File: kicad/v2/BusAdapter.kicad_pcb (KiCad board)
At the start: 2 copper layers, 99.1 x 99.1 mm, 55 parts, among them J1 Conn_02x17_Odd_Even, J10 Conn_02x06_Odd_Even, J11 Conn_02x02_Odd_Even, J12 Conn_02x06_Top_Bottom, J13 Conn_01x03, J14 Conn_01x02, J2 Conn_02x20_Odd_Even, J3 Conn_02x20_Odd_Even, J4 Conn_02x06_Top_Bottom, J5 Conn_02x06_Top_Bottom, J6 Conn_Coaxial, J7 Conn_Coaxial, J8 Conn_01x02_Male, J9 Conn_01x02_Male, Q1 2N3904, Q2 2N3904, SW1 SW_Push, SW2 SW_Push, U1 74LVC245, U2 74LVC245, U3 74LVC245, U4 IS61C5128AL-10TLI, U5 MCP4822

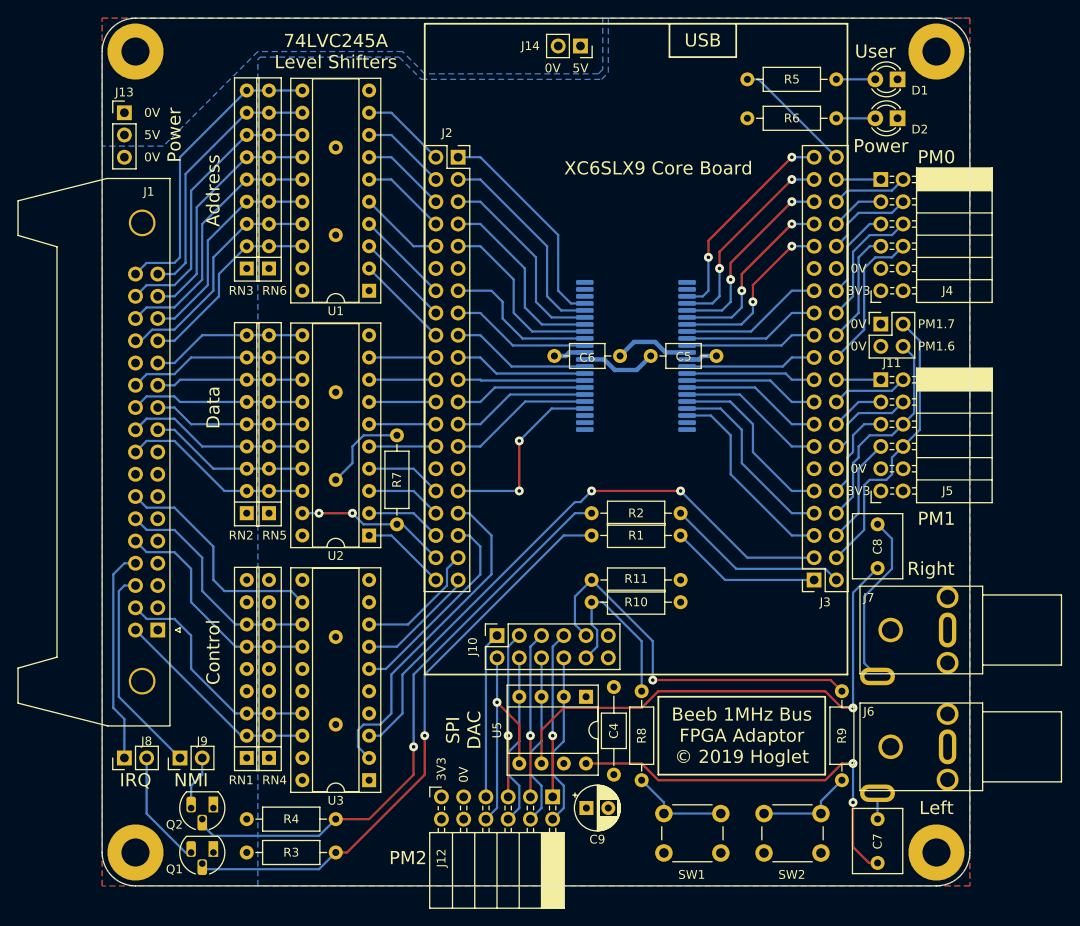
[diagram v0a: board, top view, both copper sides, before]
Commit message: PCB v2: Solder Mask Clearance/Width = 0.15mm/0.40mm
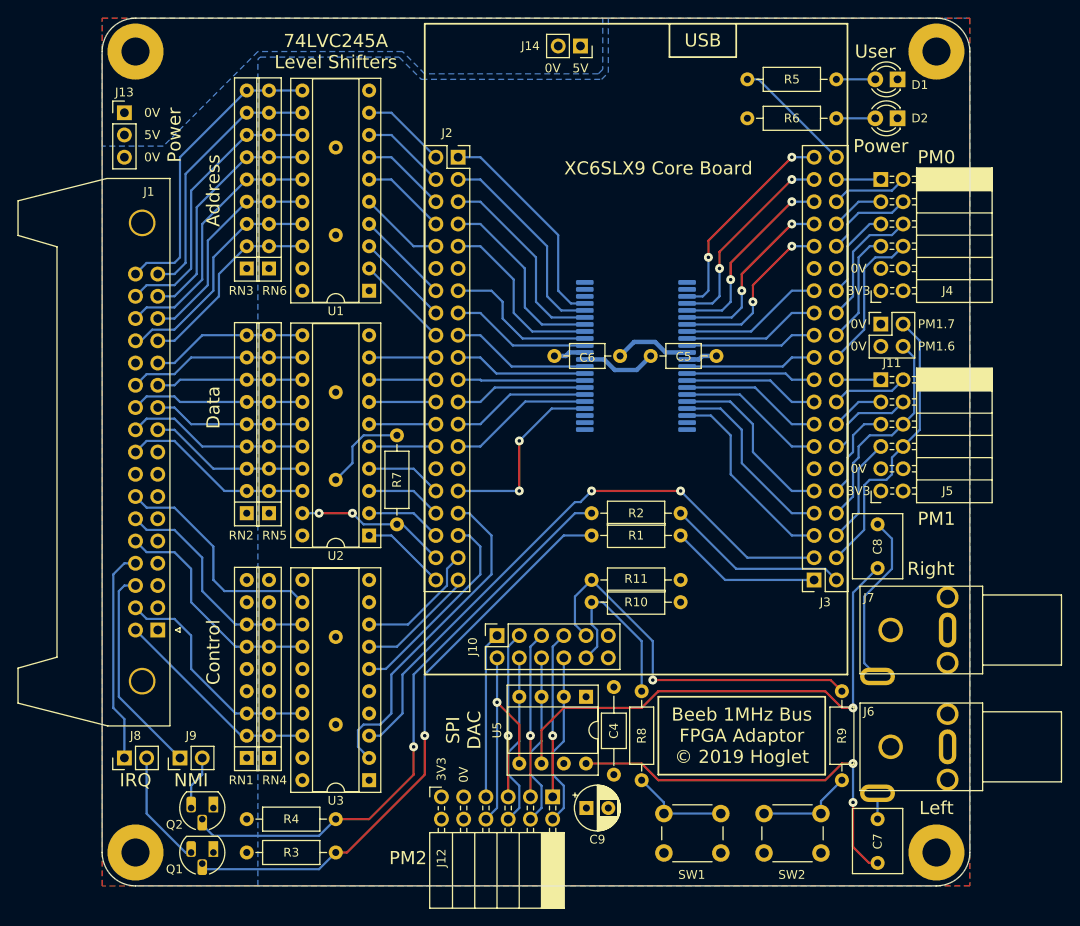
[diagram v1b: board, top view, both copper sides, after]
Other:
- rule pad_to_mask_clearance: 0.051 -> 0.15
- rule solder_mask_min_width: 0.25 -> 0.4
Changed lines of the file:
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@@
     (pad_size 1.524 1.524)
     (pad_drill 0.762)
-    (pad_to_mask_clearance 0.051)
-    (solder_mask_min_width 0.25)
+    (pad_to_mask_clearance 0.15)
+    (solder_mask_min_width 0.4)
     (aux_axis_origin 50.47 148.895)
     (grid_origin 100 100)
@@
     (descr "Through hole straight pin header, 1x02, 2.54mm pitch, single row")
     (tags "Through hole pin header THT 1x02 2.54mm single row")
-    (fp_text reference J8 (at 1.905 2.54 180) (layer F.SilkS)
+    (fp_text reference J8 (at 2.54 1.27 180) (layer F.SilkS)
       (effects (font (size 1 1) (thickness 0.15)))
     )
@@
     (descr "Through hole straight pin header, 1x02, 2.54mm pitch, single row")
     (tags "Through hole pin header THT 1x02 2.54mm single row")
-    (fp_text reference J9 (at 1.905 2.54 180) (layer F.SilkS)
+    (fp_text reference J9 (at 2.54 1.27 180) (layer F.SilkS)
       (effects (font (size 1 1) (thickness 0.15)))
     )
@@
     (descr "LED, diameter 3.0mm, 2 pins")
     (tags "LED diameter 3.0mm 2 pins")
-    (fp_text reference D1 (at -2.54 -1.27 180) (layer F.SilkS)
+    (fp_text reference D1 (at -2.54 -0.635 180) (layer F.SilkS)
       (effects (font (size 1 1) (thickness 0.15)))
     )
@@
     (descr "LED, diameter 3.0mm, 2 pins")
     (tags "LED diameter 3.0mm 2 pins")
-    (fp_text reference D2 (at -2.54 -1.27 180) (layer F.SilkS)
-      (effects (font (size 1 1) (thickness 0.15)))
-    )
+    (fp_text reference D2 (at -2.54 0 180) (layer F.SilkS)
+      (effects (font (size 1 1) (thickness 0.15)))
+    )

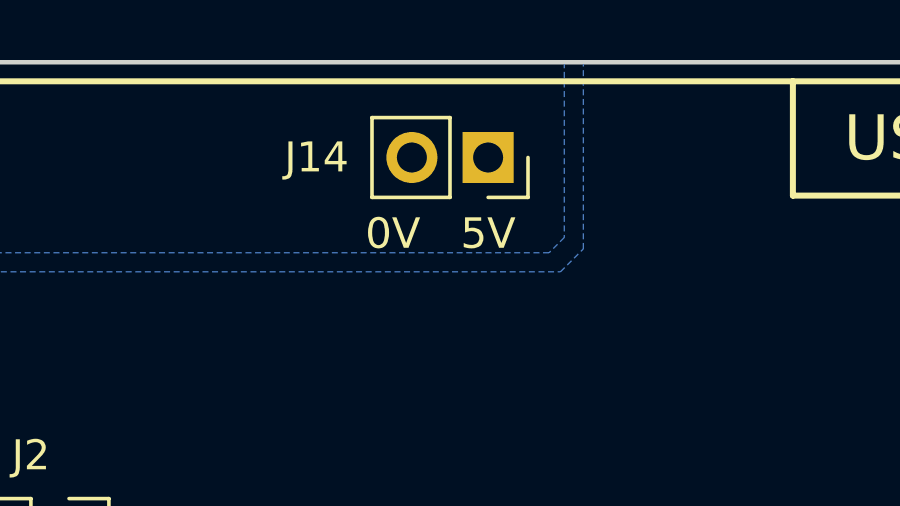
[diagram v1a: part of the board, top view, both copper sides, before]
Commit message: PCB v2: Corrected error with orientation of power connector
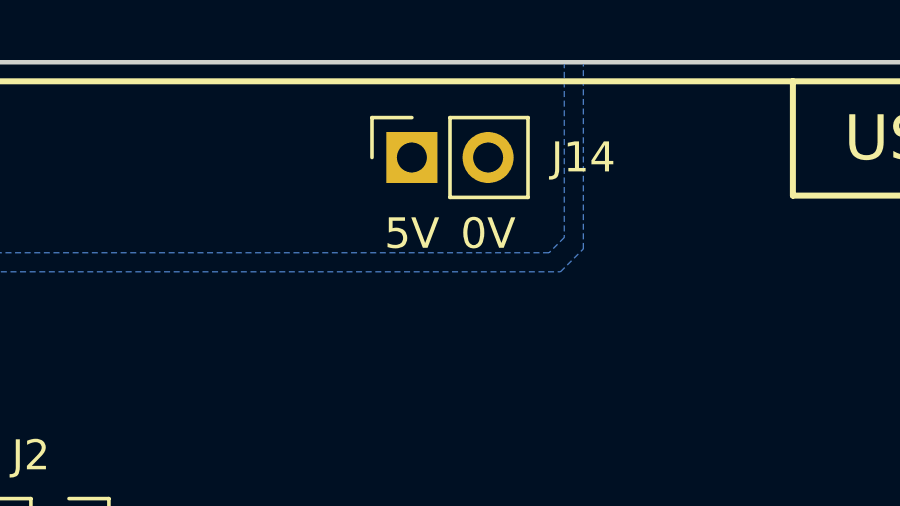
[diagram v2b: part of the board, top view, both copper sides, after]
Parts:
- moved J14 2.54 mm to (102.5, 53.0), turned to 90 degrees
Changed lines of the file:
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@@
   )
   (module Connector_PinSocket_2.54mm:PinSocket_1x02_P2.54mm_Vertical (layer F.Cu)
-    (at 105.08 53.01 270)
+    (at 102.54 53.01 90)
     (descr "Through hole straight socket strip, 1x02, 2.54mm pitch, single row (from Kicad 4.0.7), script generated")
     (tags "Through hole socket strip THT 1x02 2.54mm single row")
-    (fp_text reference J14 (at 0 5.715) (layer F.SilkS)
-      (effects (font (size 1 1) (thickness 0.15)))
-    )
-    (fp_text value Conn_01x02 (at 0 5.31 270) (layer F.Fab)
+    (fp_text reference J14 (at 0 5.715 -180) (layer F.SilkS)
+      (effects (font (size 1 1) (thickness 0.15)))
+    )
+    (fp_text value Conn_01x02 (at 0 5.31 90) (layer F.Fab)
       (effects (font (size 1 1) (thickness 0.15)))
     )
@@
     (fp_line (start 1.75 4.3) (end -1.8 4.3) (layer F.CrtYd) (width 0.05))
     (fp_line (start -1.8 4.3) (end -1.8 -1.8) (layer F.CrtYd) (width 0.05))
-    (fp_text user %R (at 0 1.27) (layer F.Fab)
-      (effects (font (size 1 1) (thickness 0.15)))
-    )
-    (pad 1 thru_hole rect (at 0 0 270) (size 1.7 1.7) (drill 1) (layers *.Cu *.Mask)
+    (fp_text user %R (at 0 1.27 -180) (layer F.Fab)
+      (effects (font (size 1 1) (thickness 0.15)))
+    )
+    (pad 1 thru_hole rect (at 0 0 90) (size 1.7 1.7) (drill 1) (layers *.Cu *.Mask)
       (net 148 +5V))
-    (pad 2 thru_hole oval (at 0 2.54 270) (size 1.7 1.7) (drill 1) (layers *.Cu *.Mask)
+    (pad 2 thru_hole oval (at 0 2.54 90) (size 1.7 1.7) (drill 1) (layers *.Cu *.Mask)
       (net 2 GND))
     (model ${KISYS3DMOD}/Connector_PinSocket_2.54mm.3dshapes/PinSocket_1x02_P2.54mm_Vertical.wrl
@@
     (effects (font (size 1.016 1.016) (thickness 0.1524)))
   )
-  (gr_text 5V (at 105.08 55.55) (layer F.SilkS)
+  (gr_text 5V (at 102.54 55.55) (layer F.SilkS)
     (effects (font (size 1.016 1.016) (thickness 0.1524)))
   )
-  (gr_text 0V (at 101.905 55.55) (layer F.SilkS)
+  (gr_text 0V (at 105.08 55.55) (layer F.SilkS)
     (effects (font (size 1.016 1.016) (thickness 0.1524)))
   )
